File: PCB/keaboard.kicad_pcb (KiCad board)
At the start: 2 copper layers, 137.2 x 88.9 mm, 78 parts, among them U1 ProMicro

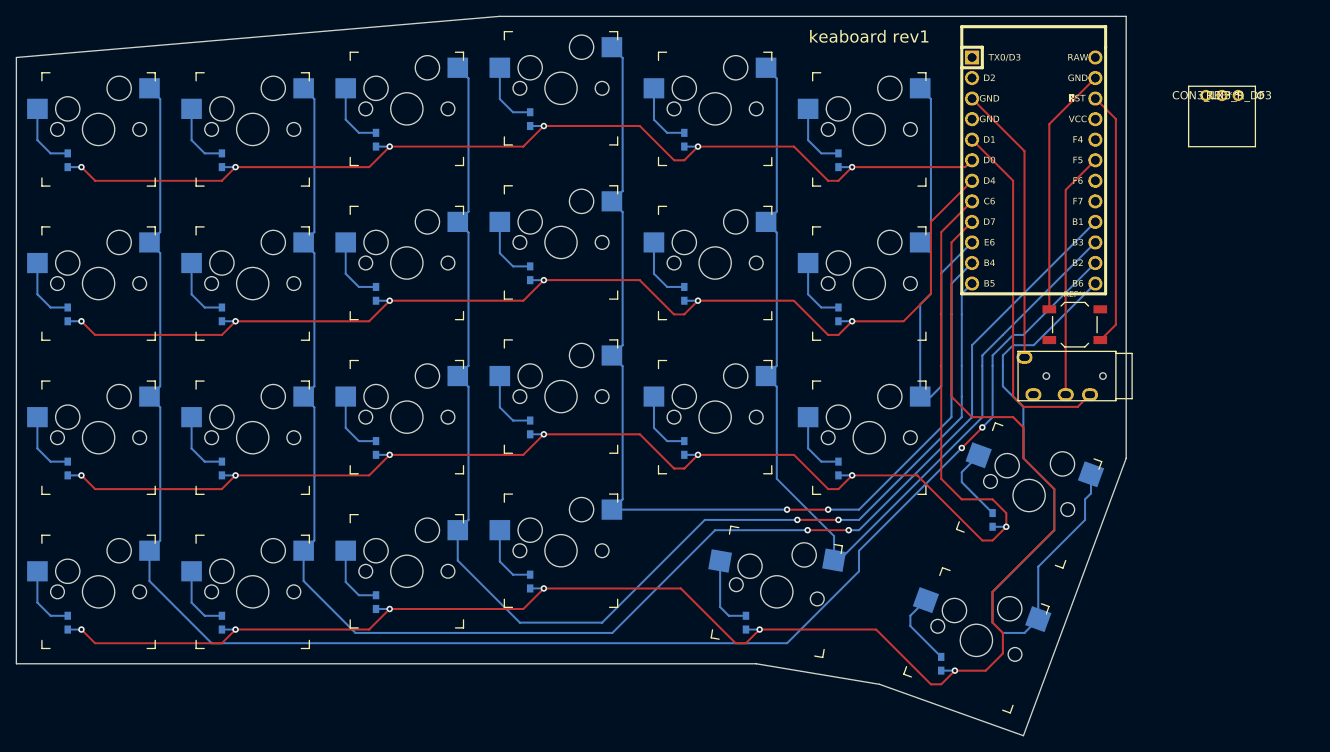
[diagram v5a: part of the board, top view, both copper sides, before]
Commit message: Reroute TRRS connection, reroute row connections, move progress images
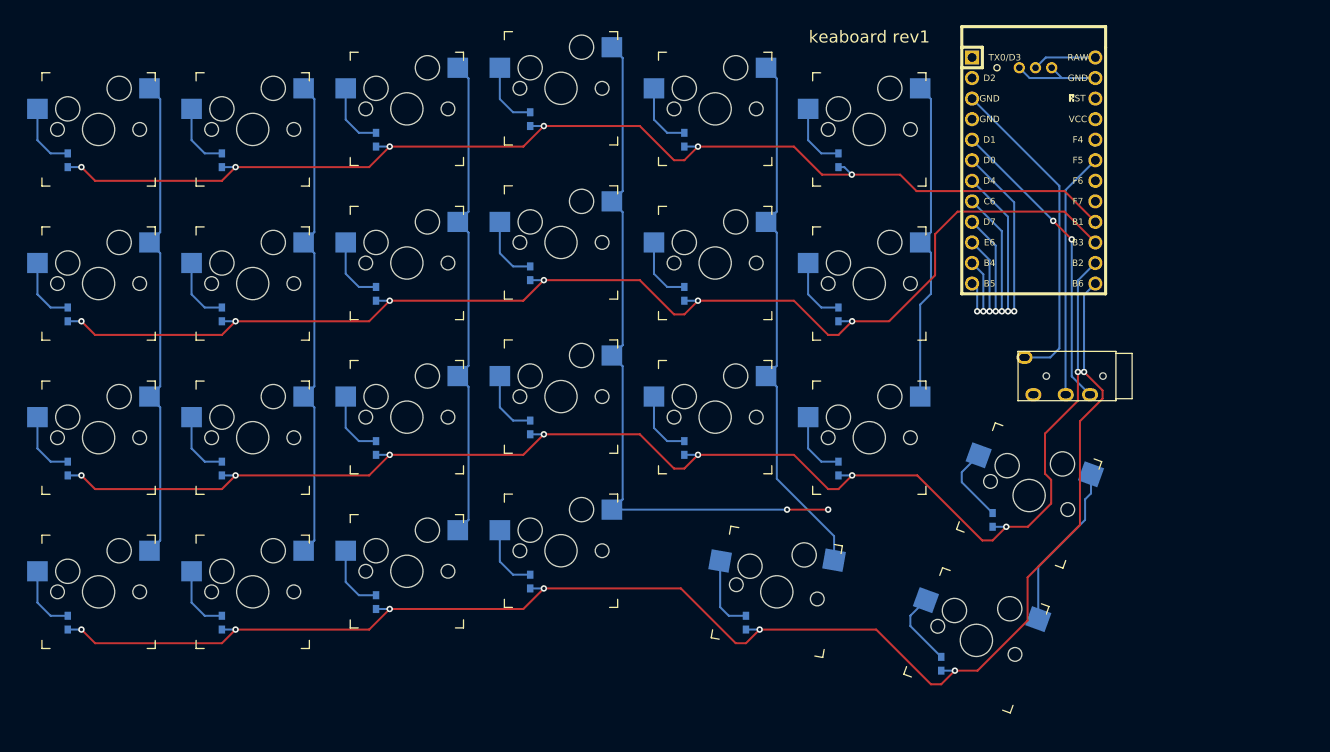
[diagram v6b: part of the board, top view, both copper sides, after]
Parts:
- removed the REF** at (171.4, 68.6)
- REF**: moved to B.Cu
- moved REF** 27.3 mm to (164.6, 36.8), turned to 180 degrees
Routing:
- net (no net): track 1990.2 -> 1486.1 mm, vias 33 -> 38
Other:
- board outline removed
- board text added: "Cover pins w/ tape"
- board text added: "GND"
- board text added: "PWR"
